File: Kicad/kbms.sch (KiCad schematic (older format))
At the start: 11 parts, among them J701 AVR-ISP-6, J702 DE9 Male, J703 DE9 Male, J704 Double-mini-DIN-6, U701 ATmega328-PU

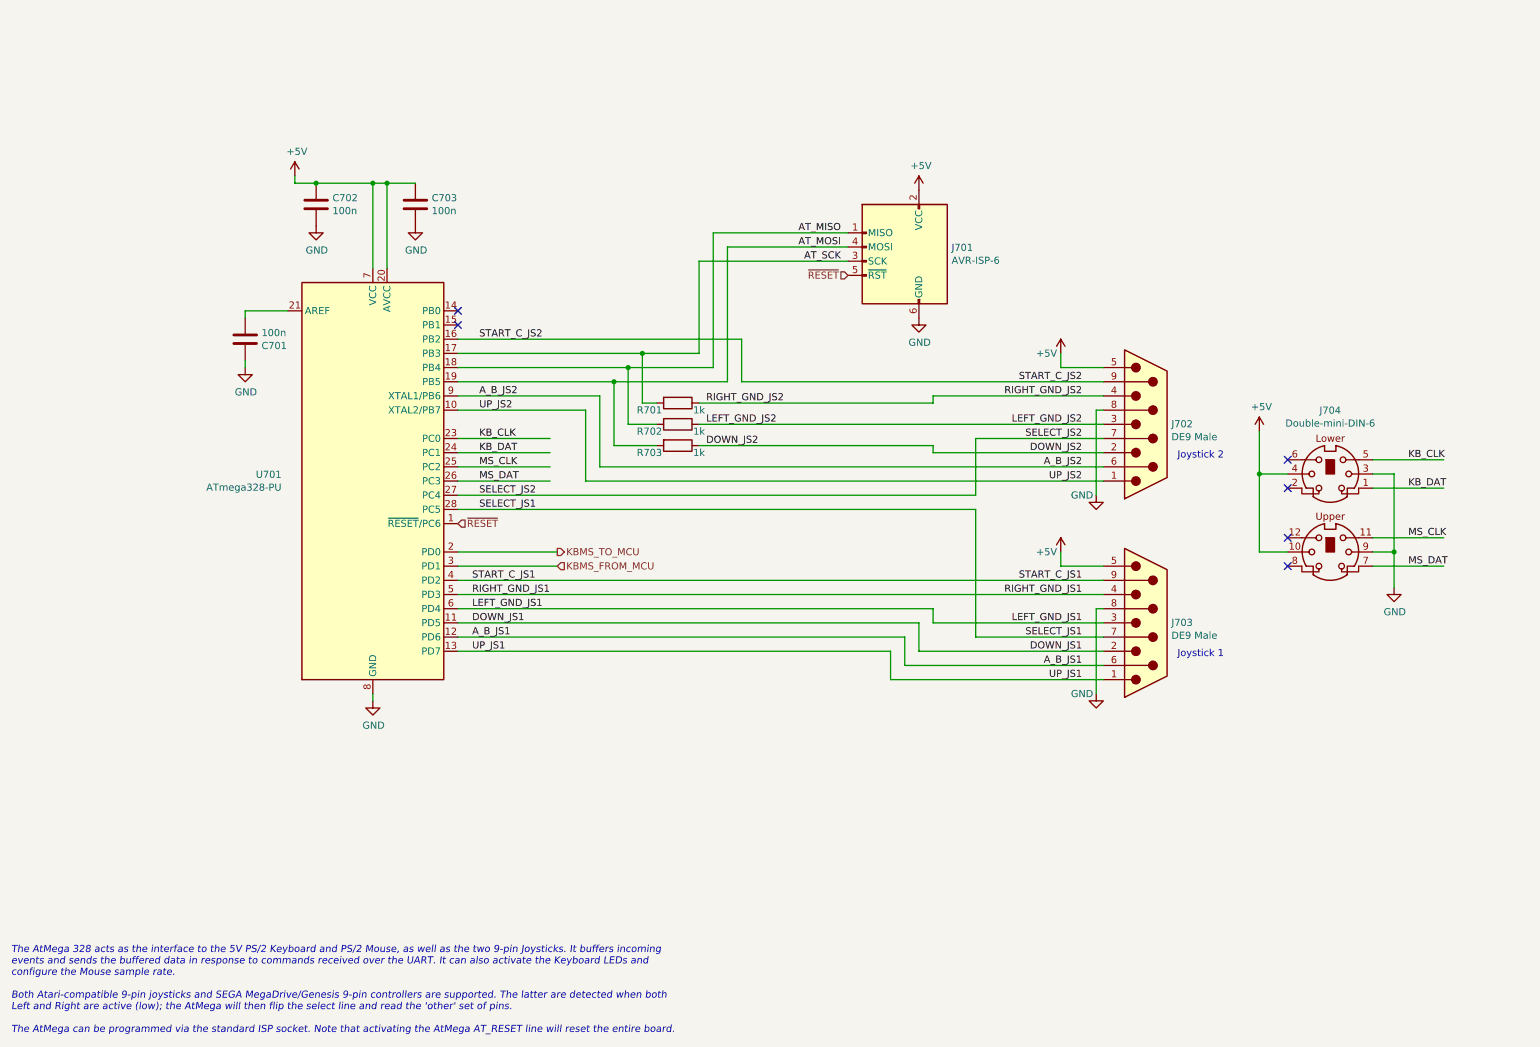
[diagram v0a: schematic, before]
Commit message: Switch to 1598D enclosure.
Use MIC2005A current limiter on input.
Use soft on/off switch from Atmega.
Atmega connects to Tiva over I2C.
Use full-size SD card.
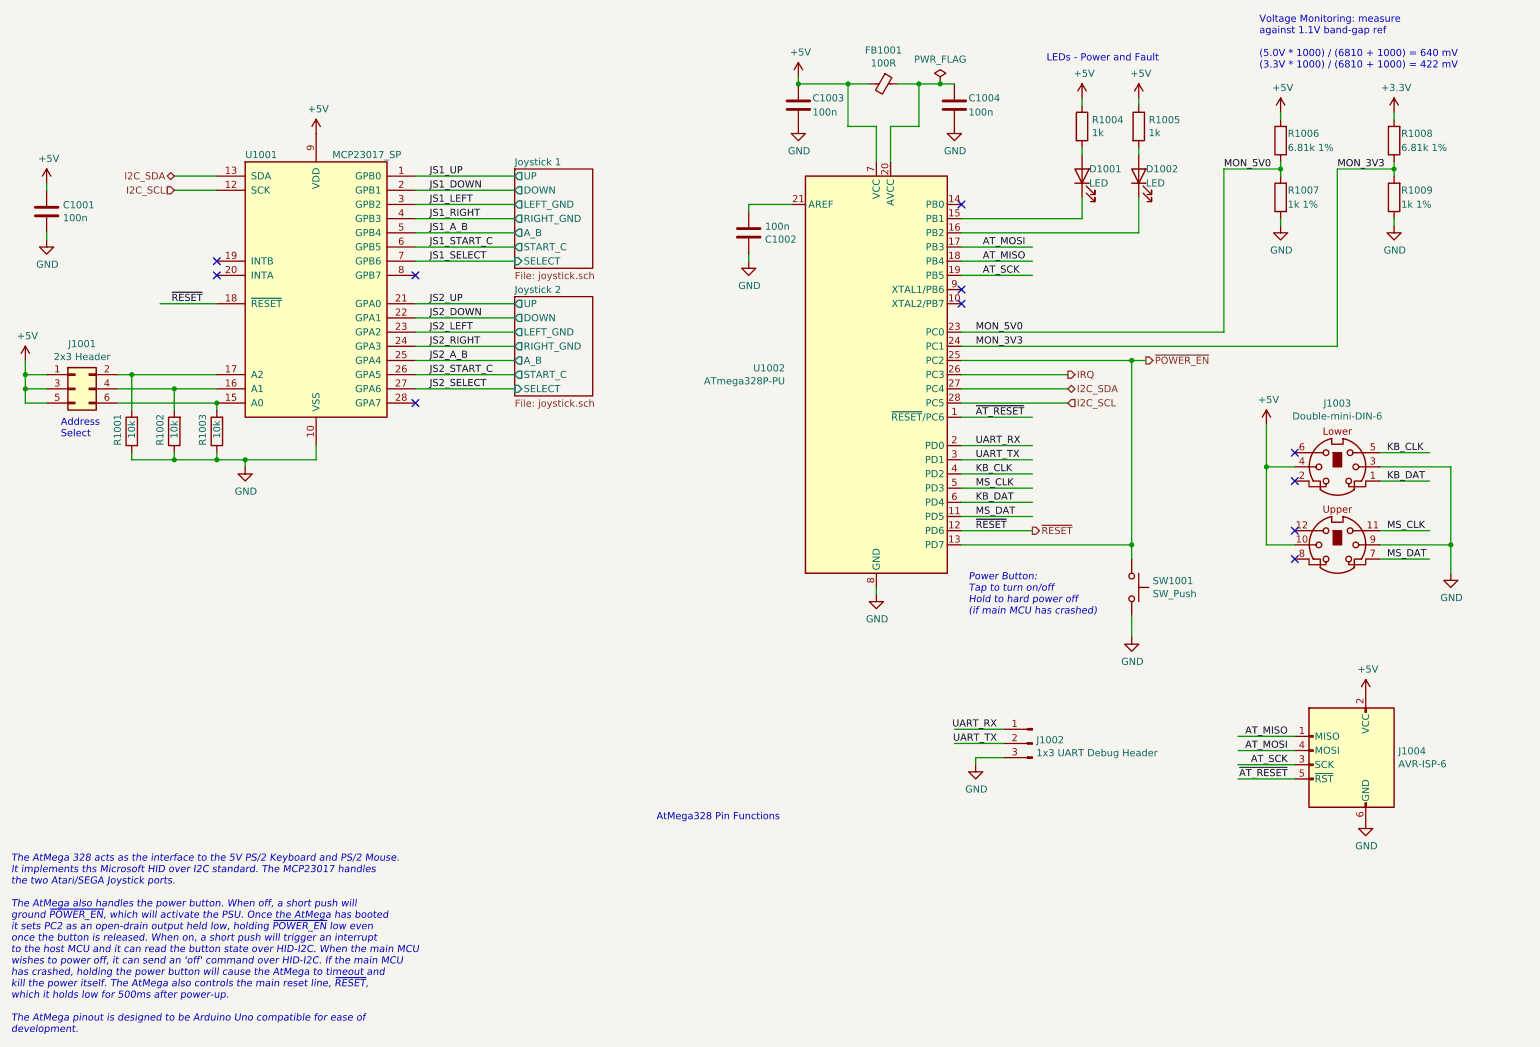
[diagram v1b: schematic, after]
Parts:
- removed C702, C703: 100n, Capacitor_THT:C_Disc_D3.0mm_W2.0mm_P2.50mm, symbol Device:C
- removed J701: AVR-ISP-6, Connector_PinHeader_2.54mm:PinHeader_2x03_P2.54mm_Vertical, symbol neotron-32-rescue:AVR-ISP-6-Connector
- removed J702, J703: DE9 Male, Connector_Dsub:DSUB-9_Male_Horizontal_P2.77x2.84mm_EdgePinOffset14.56mm_Housed_MountingHolesOffset8.20mm, symbol Connector:DB9_Male
- removed R701, R702, R703: 1k, Resistor_THT:R_Axial_DIN0207_L6.3mm_D2.5mm_P10.16mm_Horizontal, symbol Device:R
- removed U701: ATmega328-PU, Package_DIP:DIP-28_W7.62mm, symbol neotron-32-rescue:ATmega328-PU-MCU_Microchip_ATmega
- added C1001, C1003, C1004: 100n, Capacitor_THT:C_Disc_D3.0mm_W2.0mm_P2.50mm, symbol Device:C
- added D1001, D1002: LED, LED_THT:LED_D3.0mm, symbol Device:LED
- added FB1001: 100R, Ferrite_THT:LairdTech_28C0236-0JW-10, symbol Device:Ferrite_Bead_Small
- added J1001: 2x3 Header, Connector_PinHeader_2.54mm:PinHeader_2x03_P2.54mm_Vertical, symbol Connector_Generic:Conn_02x03_Odd_Even
- added J1002: 1x3 UART Debug Header, Connector_PinHeader_2.54mm:PinHeader_1x03_P2.54mm_Vertical, symbol Connector:Conn_01x03_Male
- added J1004: AVR-ISP-6, Connector_PinHeader_2.54mm:PinHeader_2x03_P2.54mm_Horizontal, symbol Connector:AVR-ISP-6
- added R1001, R1002, R1003: 10k, Resistor_THT:R_Axial_DIN0207_L6.3mm_D2.5mm_P10.16mm_Horizontal, symbol Device:R
- added R1004, R1005: 1k, Resistor_THT:R_Axial_DIN0207_L6.3mm_D2.5mm_P10.16mm_Horizontal, symbol Device:R
- added R1006, R1008: 6.81k 1%, Resistor_THT:R_Axial_DIN0207_L6.3mm_D2.5mm_P10.16mm_Horizontal, symbol Device:R
- added R1007, R1009: 1k 1%, Resistor_THT:R_Axial_DIN0207_L6.3mm_D2.5mm_P10.16mm_Horizontal, symbol Device:R
- added SW1001: SW_Push, Neotron 32:PHB2UEETS1A, symbol Switch:SW_Push
- added U1001: MCP23017_SP, Package_DIP:DIP-28_W7.62mm, symbol Interface_Expansion:MCP23017_SP
- added U1002: ATmega328P-PU, Package_DIP:DIP-28_W7.62mm, symbol MCU_Microchip_ATmega:ATmega328P-PU
- renumbered C701 to C1002, J704 to J1003
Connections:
- net labels added: +3.3V, I2C_SCL, I2C_SDA, IRQ, JS1_A_B, JS1_DOWN, JS1_LEFT, JS1_RIGHT, JS1_SELECT, JS1_START_C, JS1_UP, JS2_A_B, JS2_DOWN, JS2_LEFT, JS2_RIGHT, JS2_SELECT, JS2_START_C, JS2_UP, MON_3V3, MON_5V0, UART_RX, UART_TX, ~AT_RESET, ~POWER_EN
- net labels removed: A_B_JS1, A_B_JS2, DOWN_JS1, DOWN_JS2, KBMS_FROM_MCU, KBMS_TO_MCU, LEFT_GND_JS1, LEFT_GND_JS2, RIGHT_GND_JS1, RIGHT_GND_JS2, SELECT_JS1, SELECT_JS2, START_C_JS1, START_C_JS2, UP_JS1, UP_JS2
- wire segments 91 -> 120
- no-connect marks 6 -> 11
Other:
- note added: "Address\nSelect"
- note added: "AtMega328 Pin Functions"
- note added: "LEDs - Power and Fault"
- note added: "Power Button:\nTap to turn on/off\nHold to hard power off\n(if main MCU has crashed)"
- note added: "The AtMega 328 acts as the interface to the 5V PS/2 Keyboard and PS/2 Mouse.\nIt implements ths Microsoft HID over I2C standard. The MCP23017 handles\nthe two Atari/SEGA Joystick ports.\n\nThe AtMega also handles the power button. When off, a short push will\nground ~POWER_EN~, which will activate the PSU. Once the AtMega has booted\nit sets PC2 as an open-drain output held low, holding ~POWER_EN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"
- note added: "Voltage Monitoring: measure\nagainst 1.1V band-gap ref\n\n(5.0V * 1000) / (6810 + 1000) = 640 mV\n(3.3V * 1000) / (6810 + 1000) = 422 mV\n"
- note removed: "Joystick 1"
- note removed: "Joystick 2"
- note removed: "The AtMega 328 acts as the interface to the 5V PS/2 Keyboard and PS/2 Mouse, as well as the two 9-pin Joysticks. It buffers incoming\nevents and sends the buffered data in response to commands received over the UART. It can also activate the Keyboard LEDs and\nconfigure the Mouse sample rate.\n\nBoth Atari-compatible 9-pin joysticks and SEGA MegaDrive/Genesis 9-pin controllers are supported. The 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"
- moved on the sheet: C1002, J1003

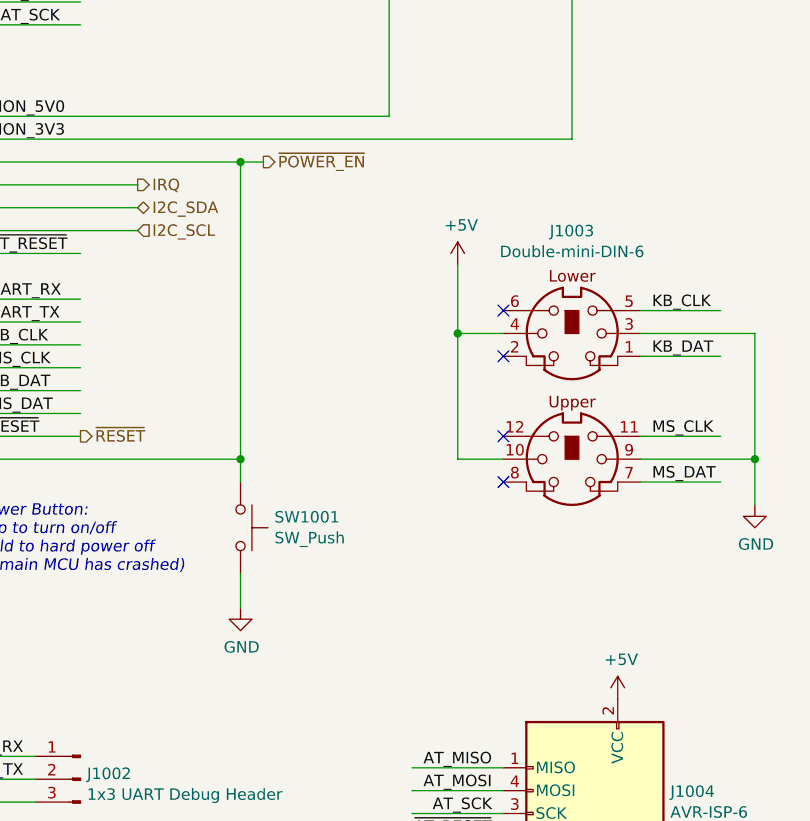
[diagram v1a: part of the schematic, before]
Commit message: Working on layout.
Laid out the parallel port - reordered some pins to make it easier.
Set the minimum track widths to 6 mil/6 mil with a 6mm/3mm via.
Replaced the SPST power switch with a PUE to match the reset switch.
Attached some existing 3D models to the PCB footprints.
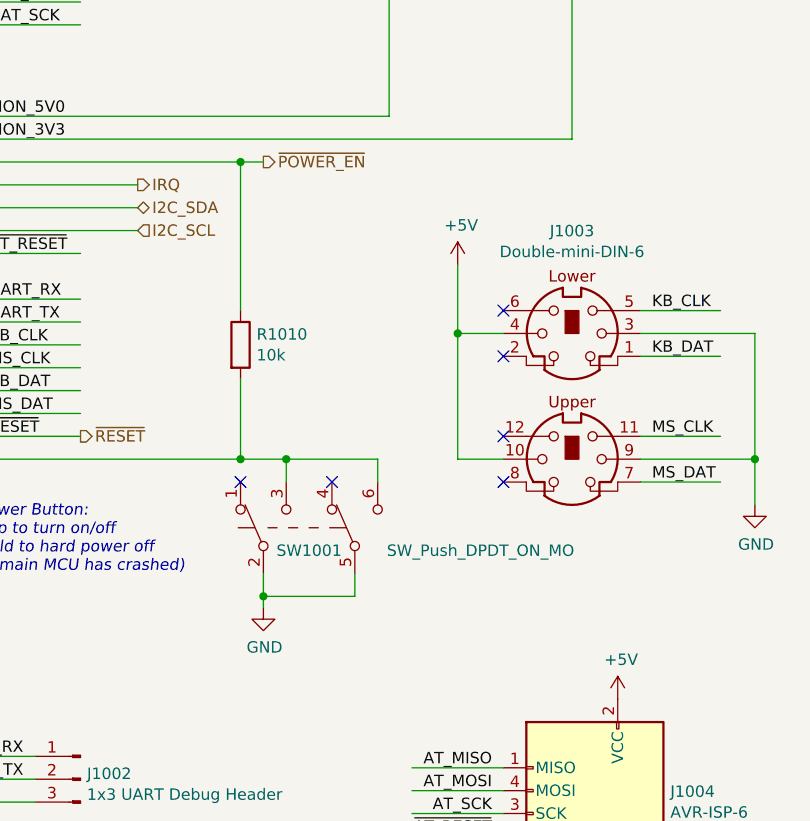
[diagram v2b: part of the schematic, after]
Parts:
- removed SW1001: SW_Push, Neotron 32:PHB2UEETS1A, symbol Switch:SW_Push
- added R1010: 10k, Resistor_THT:R_Axial_DIN0207_L6.3mm_D2.5mm_P10.16mm_Horizontal, symbol Device:R
- added SW1001: SW_Push_DPDT_ON_MO, Neotron 32:PHB2UEETS1A, symbol Switch:SW_Push_DPDT
- J1004: footprint Connector_PinHeader_2.54mm:PinHeader_2x03_P2.54mm_Horizontal -> Connector_PinHeader_2.54mm:PinHeader_2x03_P2.54mm_Vertical
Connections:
- wire segments 120 -> 127
- no-connect marks 11 -> 13
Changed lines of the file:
@@
 ~POWER_EN
 $Comp
-L Switch:SW_Push SW1001
-U 1 1 5F570471
-P 8450 4550
-F 0 "SW1001" V 8404 4698 50  0000 L CNN
-F 1 "SW_Push" V 8495 4698 50  0000 L CNN
-F 2 "Neotron 32:PHB2UEETS1A" H 8450 4750 50  0001 C CNN
-F 3 "~" H 8450 4750 50  0001 C CNN
-	1    8450 4550
-	0    1    1    0
-$EndComp
-Wire Wire Line
-	8450 4250 8450 4350
-$Comp
 L power:GND #PWR?
 U 1 1 5F57B3A4
-P 8450 4900
+P 8550 4900
 AR Path="/5F57B3A4" Ref="#PWR?"  Part="1"
 AR Path="/5DF2662E/5F57B3A4" Ref="#PWR?"  Part="1"
-F 0 "#PWR?" H 8450 4650 50  0001 C CNN
-F 1 "GND" H 8455 4727 50  0000 C CNN
-F 2 "" H 8450 4900 50  0001 C CNN
-F 3 "" H 8450 4900 50  0001 C CNN
-	1    8450 4900
+F 0 "#PWR?" H 8550 4650 50  0001 C CNN
+F 1 "GND" H 8555 4727 50  0000 C CNN
+F 2 "" H 8550 4900 50  0001 C CNN
+F 3 "" H 8550 4900 50  0001 C CNN
+	1    8550 4900
 	1    0    0    -1
 $EndComp
@@
 	7250 2950 8450 2950
 Wire Wire Line
-	8450 4250 8450 2950
+	8450 4250 8450 3900
 Connection ~ 8450 2950
 Wire Wire Line
 	8450 2950 8550 2950
-Connection ~ 8450 4250
 Wire Wire Line
 	7250 4250 8450 4250
 Wire Wire Line
-	8450 4900 8450 4750
+	8550 4900 8550 4850
 $Bitmap
 Pos 5600 6950
@@
 F 0 "J1004" H 9670 5896 50  0000 R CNN
 F 1 "AVR-ISP-6" H 9670 5805 50  0000 R CNN
-F 2 "Connector_PinHeader_2.54mm:PinHeader_2x03_P2.54mm_Horizontal" V 9750 5850 50  0001 C CNN
+F 2 "Connector_PinHeader_2.54mm:PinHeader_2x03_P2.54mm_Vertical" V 9750 5850 50  0001 C CNN
 F 3 " ~" H 8725 5250 50  0001 C CNN
 	1    10000 5800
 	-1   0    0    -1
 $EndComp
+$Comp
+L Switch:SW_Push_DPDT SW?
+U 1 1 5F4081CD
+P 8750 4550
+AR Path="/5DF5D5D7/5F4081CD" Ref="SW?"  Part="1"
+AR Path="/5DF2662E/5F4081CD" Ref="SW1001"  Part="1"
+F 0 "SW1001" V 8650 4550 50  0000 C CNN
+F 1 "SW_Push_DPDT_ON_MO" V 8650 3800 50  0000 C CNN
+F 2 "Neotron 32:PHB2UEETS1A" H 8750 4750 50  0001 C CNN
+F 3 "~" H 8750 4750 50  0001 C CNN
+F 4 "C&K" H 8750 4550 50  0001 C CNN "Manufacturer"
+F 5 "PHB2UOATS1A" H 8750 4550 50  0001 C CNN "mpn"
+F 6 "0" H 8750 4550 50  0001 C CNN "DNP"
+	1    8750 4550
+	0    -1   -1   0
+$EndComp
+Wire Wire Line
+	8550 4850 8950 4850
+Wire Wire Line
+	8950 4850 8950 4750
+Connection ~ 8550 4850
+Wire Wire Line
+	8550 4850 8550 4750
+Wire Wire Line
+	8450 4250 8650 4250
+Wire Wire Line
+	8650 4250 8650 4350
+Connection ~ 8450 4250
+Wire Wire Line
+	9050 4250 9050 4350
+Wire Wire Line
+	8650 4250 9050 4250
+Connection ~ 8650 4250
+$Comp
+L Device:R R1010
+U 1 1 5F427BC4
+P 8450 3750
+F 0 "R1010" H 8520 3796 50  0000 L CNN
+F 1 "10k" H 8520 3705 50  0000 L CNN
+F 2 "Resistor_THT:R_Axial_DIN0207_L6.3mm_D2.5mm_P10.16mm_Horizontal" V 8380 3750 50  0001 C CNN
+F 3 "~" H 8450 3750 50  0001 C CNN
+	1    8450 3750
+	1    0    0    -1
+$EndComp
+Wire Wire Line
+	8450 3600 8450 2950
+NoConn ~ 8850 4350
+NoConn ~ 8450 4350
 $EndSCHEMATC
